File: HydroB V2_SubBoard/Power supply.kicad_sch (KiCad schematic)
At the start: 16 parts, among them J2 Conn_01x02_Pin, U2 TPS5410D, U4 TPS7A2633DRVR

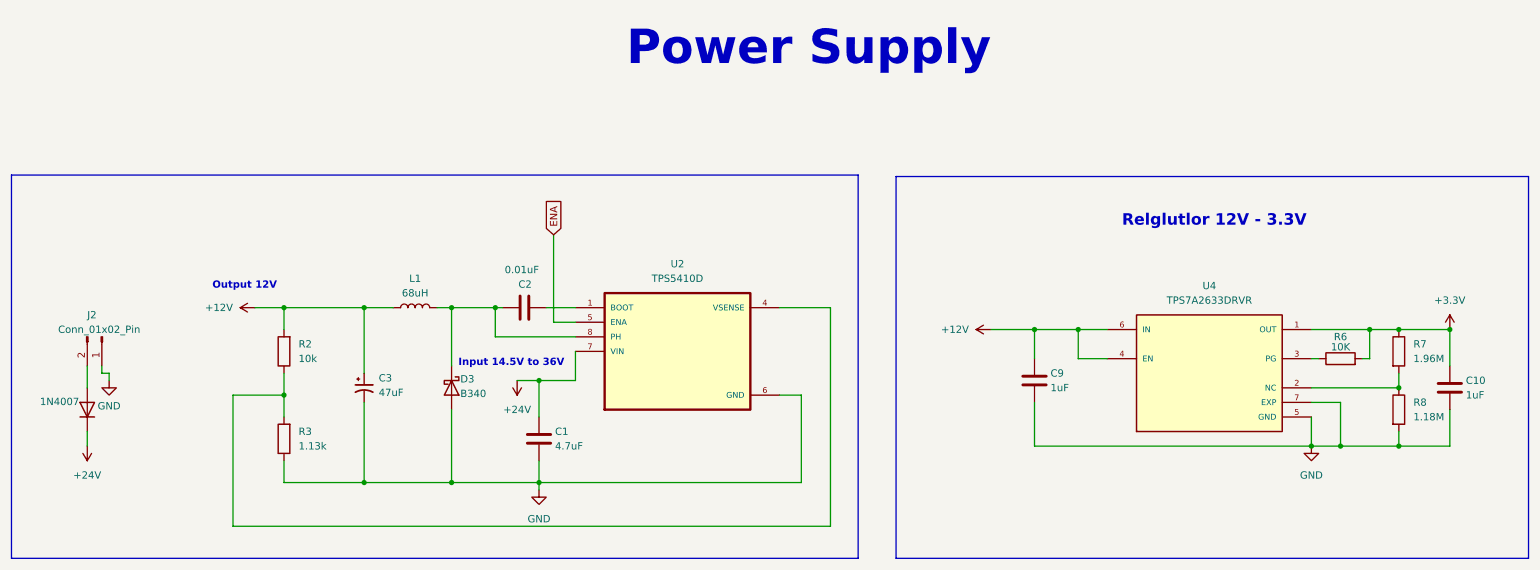
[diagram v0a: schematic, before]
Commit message: the schematic of sub-board updated
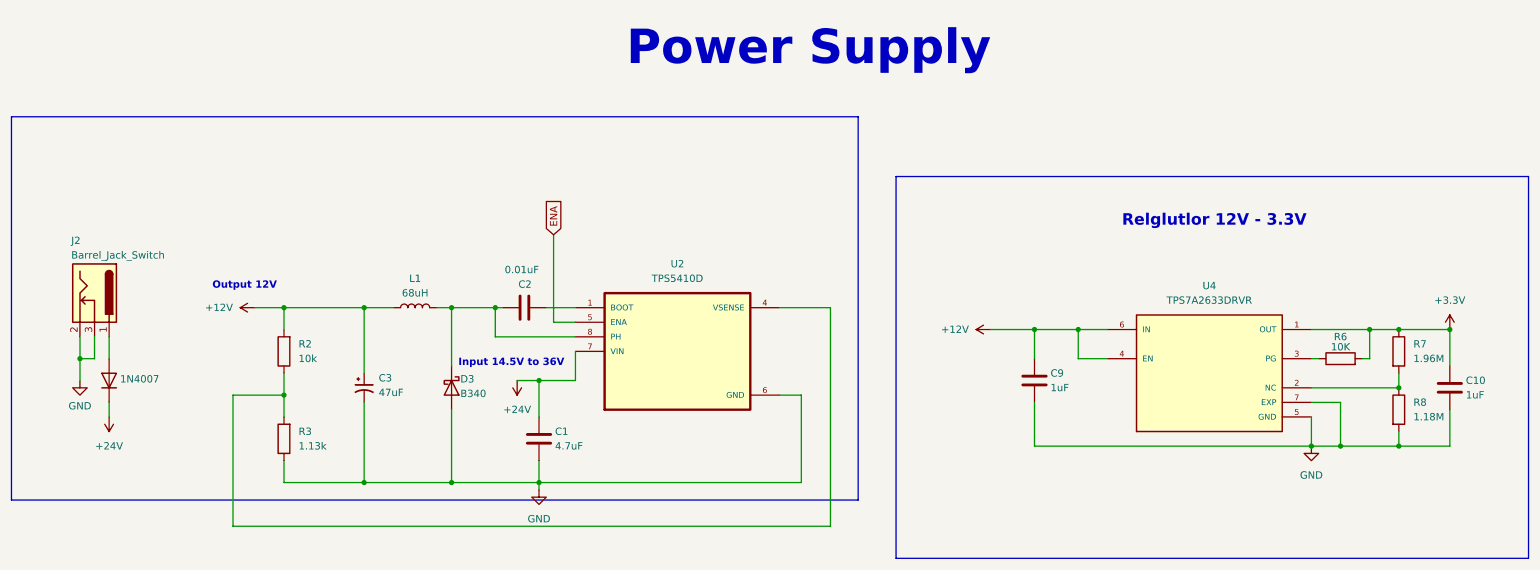
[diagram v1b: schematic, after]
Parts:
- removed J2: Conn_01x02_Pin, Connector_Phoenix_MC:PhoenixContact_MCV_1,5_2-G-3.5_1x02_P3.50mm_Vertical, symbol Connector:Conn_01x02_Pin
- added J2: Barrel_Jack_Switch, Connector_BarrelJack:BarrelJack_Horizontal, symbol Connector:Barrel_Jack_Switch
- C9: footprint Capacitor_SMD:C_0603_1608Metric -> Capacitor_SMD:C_0805_2012Metric
- D3: footprint Diode_SMD:D_SMC -> Diode_SMD:D_SMA
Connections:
- net GND: now also J2.2, J2.3
- net at D2.2 (A): now also J2.1
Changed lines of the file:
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@@
 	)
 	(junction
+		(at 25.4 77.47)
+		(diameter 0)
+		(color 0 0 0 0)
+	)
+	(junction
 		(at 191.77 72.39)
 		(diameter 0)
@@
 	(wire
 		(pts
-			(xy 26.67 90.17) (xy 26.67 92.71)
+			(xy 30.48 85.09) (xy 30.48 87.63)
 		)
 		(stroke
@@
 	(wire
 		(pts
-			(xy 250.19 72.39) (xy 250.19 77.47)
+			(xy 27.94 73.66) (xy 27.94 77.47)
 		)
 		(stroke
@@
 	(wire
 		(pts
-			(xy 240.03 72.39) (xy 250.19 72.39)
+			(xy 250.19 72.39) (xy 250.19 77.47)
 		)
 		(stroke
@@
 	(wire
 		(pts
-			(xy 74.93 99.06) (xy 90.17 99.06)
+			(xy 240.03 72.39) (xy 250.19 72.39)
 		)
 		(stroke
@@
 	(wire
 		(pts
-			(xy 30.48 80.01) (xy 29.21 80.01)
+			(xy 74.93 99.06) (xy 90.17 99.06)
 		)
 		(stroke
@@
 	(wire
 		(pts
+			(xy 25.4 77.47) (xy 25.4 81.28)
+		)
+		(stroke
+			(width 0)
+			(type default)
+		)
+	)
+	(wire
+		(pts
 			(xy 255.27 80.01) (xy 255.27 82.55)
 		)
@@
 	(wire
 		(pts
-			(xy 29.21 80.01) (xy 29.21 78.74)
+			(xy 25.4 73.66) (xy 25.4 77.47)
 		)
 		(stroke
@@
 	(wire
 		(pts
-			(xy 30.48 80.01) (xy 30.48 81.28)
+			(xy 27.94 77.47) (xy 25.4 77.47)
 		)
 		(stroke
@@
 	(wire
 		(pts
-			(xy 26.67 78.74) (xy 26.67 82.55)
+			(xy 30.48 73.66) (xy 30.48 77.47)
 		)
 		(stroke
@@
 	)
 	(rectangle
-		(start 13.462 45.466)
-		(end 161.036 112.268)
+		(start 13.462 35.306)
+		(end 161.036 102.108)
 		(stroke
 			(width 0)
@@
 	(symbol
 		(lib_id "power:GND")
-		(at 30.48 81.28 0)
+		(at 25.4 81.28 0)
 		(unit 1)
 		(exclude_from_sim no)
@@
 		(fields_autoplaced yes)
 		(property "Reference" "#PWR04"
-			(at 30.48 87.63 0)
+			(at 25.4 87.63 0)
 			(effects
 				(font
@@
 		)
 		(property "Value" "GND"
-			(at 30.48 85.725 0)
+			(at 25.4 85.725 0)
 			(effects
 				(font
@@
 		)
 		(property "Footprint" ""
-			(at 30.48 81.28 0)
+			(at 25.4 81.28 0)
 			(effects
 				(font
@@
 		)
 		(property "Datasheet" ""
-			(at 30.48 81.28 0)
+			(at 25.4 81.28 0)
 			(effects
 				(font
@@
 		)
 		(property "Description" ""
-			(at 30.48 81.28 0)
+			(at 25.4 81.28 0)
 			(effects
 				(font
@@
 	)
 	(symbol
-		(lib_id "Connector:Conn_01x02_Pin")
-		(at 29.21 73.66 270)
-		(unit 1)
-		(exclude_from_sim no)
-		(in_bom yes)
-		(on_board yes)
-		(dnp no)
-		(property "Reference" "J2"
-			(at 26.67 69.85 90)
-			(effects
-				(font
-					(size 1.27 1.27)
-				)
-				(justify left)
-			)
-		)
-		(property "Value" "Conn_01x02_Pin"
-			(at 21.59 72.39 90)
-			(effects
-				(font
-					(size 1.27 1.27)
-				)
-				(justify left)
-			)
-		)
-		(property "Footprint" "Connector_Phoenix_MC:PhoenixContact_MCV_1,5_2-G-3.5_1x02_P3.50mm_Vertical"
-			(at 29.21 73.66 0)
-			(effects
-				(font
-					(size 1.27 1.27)
-				)
-				(hide yes)
-			)
-		)
-		(property "Datasheet" "~"
-			(at 29.21 73.66 0)
-			(effects
-				(font
-					(size 1.27 1.27)
-				)
-				(hide yes)
-			)
-		)
-		(property "Description" "Generic connector, single row, 01x02, script generated"
-			(at 29.21 73.66 0)
-			(effects
-				(font
-					(size 1.27 1.27)
-				)
-				(hide yes)
-			)
-		)
-		(pin "2"
-		)
-		(pin "1"
-		)
-		(instances
-			(project "HydroB V2"
-				(path "/0a8bb8df-6bdd-4d10-933b-144d3fa4f517/b5cea501-254b-4c6a-af47-d8c013c279ab/d50825f3-7645-4f22-8c9c-6a6002c3efba"
-					(reference "J2")
-					(unit 1)
-				)
-			)
-		)
-	)
-	(symbol
 		(lib_id "Diode:B340")
 		(at 90.17 82.55 270)
@@
 			)
 		)
-		(property "Footprint" "Diode_SMD:D_SMC"
+		(property "Footprint" "Diode_SMD:D_SMA"
 			(at 85.725 82.55 0)
 			(effects
@@
 	(symbol
 		(lib_id "Device:D")
-		(at 26.67 86.36 90)
+		(at 30.48 81.28 90)
 		(unit 1)
 		(exclude_from_sim no)
@@
 		(dnp no)
 		(property "Reference" "D2"
-			(at 21.844 87.503 90)
+			(at 25.654 82.423 90)
 			(effects
 				(font
@@
 		)
 		(property "Value" "1N4007"
-			(at 21.844 84.963 90)
+			(at 35.814 81.026 90)
 			(effects
 				(font
@@
 		)
 		(property "Footprint" "Diode_SMD:D_SMA"
-			(at 26.67 86.36 0)
+			(at 30.48 81.28 0)
 			(effects
 				(font
@@
 		)
 		(property "Datasheet" "~"
-			(at 26.67 86.36 0)
+			(at 30.48 81.28 0)
 			(effects
 				(font
@@
 		)
 		(property "Description" ""
-			(at 26.67 86.36 0)
+			(at 30.48 81.28 0)
 			(effects
 				(font
@@
 	)
 	(symbol
+		(lib_id "Connector:Barrel_Jack_Switch")
+		(at 27.94 66.04 270)
+		(unit 1)
+		(exclude_from_sim no)
+		(in_bom yes)
+		(on_board yes)
+		(dnp no)
+		(property "Reference" "J2"
+			(at 23.876 56.896 90)
+			(effects
+				(font
+					(size 1.27 1.27)
+				)
+				(justify left)
+			)
+		)
+		(property "Value" "Barrel_Jack_Switch"
+			(at 23.876 59.436 90)
+			(effects
+				(font
+					(size 1.27 1.27)
+				)
+				(justify left)
+			)
+		)
+		(property "Footprint" "Connector_BarrelJack:BarrelJack_Horizontal"
+			(at 26.924 67.31 0)
+			(effects
+				(font
+					(size 1.27 1.27)
+				)
+				(hide yes)
+			)
+		)
+		(property "Datasheet" "~"
+			(at 26.924 67.31 0)
+			(effects
+				(font
+					(size 1.27 1.27)
+				)
+				(hide yes)
+			)
+		)
+		(property "Description" "DC Barrel Jack with an internal switch"
+			(at 27.94 66.04 0)
+			(effects
+				(font
+					(size 1.27 1.27)
+				)
+				(hide yes)
+			)
+		)
+		(pin "2"
+		)
+		(pin "1"
+		)
+		(pin "3"
+		)
+		(instances
+			(project "HydroB V2"
+				(path "/0a8bb8df-6bdd-4d10-933b-144d3fa4f517/b5cea501-254b-4c6a-af47-d8c013c279ab/d50825f3-7645-4f22-8c9c-6a6002c3efba"
+					(reference "J2")
+					(unit 1)
+				)
+			)
+		)
+	)
+	(symbol
 		(lib_id "power:GND")
 		(at 240.03 92.71 0)
@@
 	(symbol
 		(lib_id "power:+24V")
-		(at 26.67 92.71 180)
+		(at 30.48 87.63 180)
 		(unit 1)
 		(exclude_from_sim no)
@@
 		(fields_autoplaced yes)
 		(property "Reference" "#PWR013"
-			(at 26.67 88.9 0)
+			(at 30.48 83.82 0)
 			(effects
 				(font
@@
 		)
 		(property "Value" "+24V"
-			(at 26.67 97.79 0)
+			(at 30.48 92.71 0)
 			(effects
 				(font
@@
 		)
 		(property "Footprint" ""
-			(at 26.67 92.71 0)
+			(at 30.48 87.63 0)
 			(effects
 				(font
@@
 		)
 		(property "Datasheet" ""
-			(at 26.67 92.71 0)
+			(at 30.48 87.63 0)
 			(effects
 				(font
@@
 		)
 		(property "Description" "Power symbol creates a global label with name \"+24V\""
-			(at 26.67 92.71 0)
+			(at 30.48 87.63 0)
 			(effects
 				(font
@@
 			)
 		)
-		(property "Footprint" "Capacitor_SMD:C_0603_1608Metric"
+		(property "Footprint" "Capacitor_SMD:C_0805_2012Metric"
 			(at 192.7352 85.09 0)
 			(effects
